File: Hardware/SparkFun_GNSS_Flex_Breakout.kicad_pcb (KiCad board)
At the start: 4 copper layers, 63.5 x 50.8 mm, 194 parts, among them J1 microSD_Friction, J10 USB_C_Receptacle, J11 Conn_02x10, J12 Conn_02x10, J13 JST_Locking_6, J14 Qwiic_Vertical, J2 SMA_Edge, J3 Conn_01x15, J4 Conn_01x18, J5 JST_Locking_6, J6 SMA_Edge, J7 USB_C_Receptacle, J8 U.FL, J9 U.FL, U1 RT9080-3.3, U2 CH342F, U3 74HC4066BQ, U4 AP7361C-3.3V, U5 74HC4066BQ

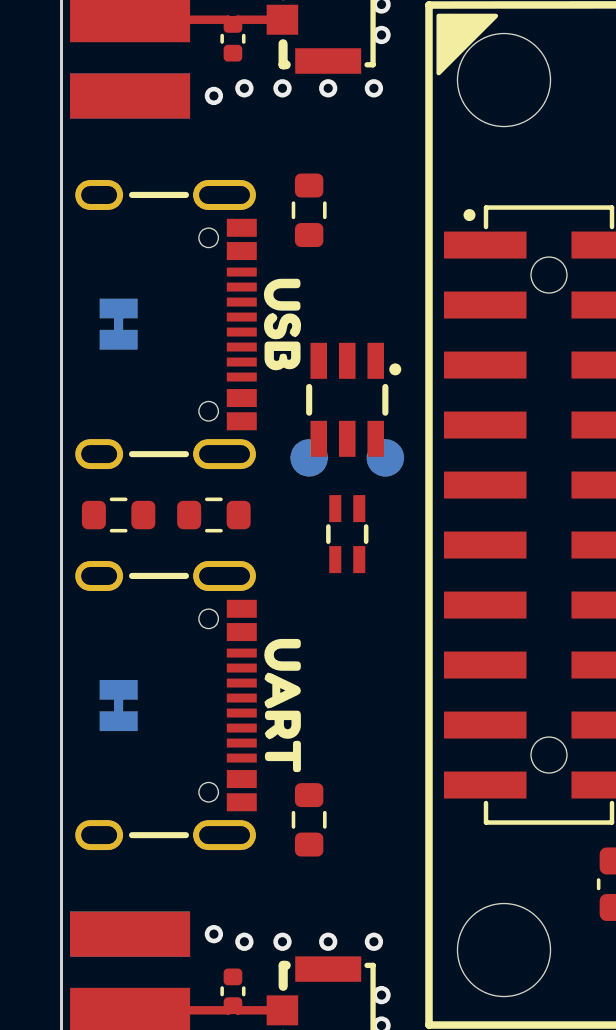
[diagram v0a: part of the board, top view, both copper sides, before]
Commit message: Update QFN-14 3D model. Nudge USB connectors
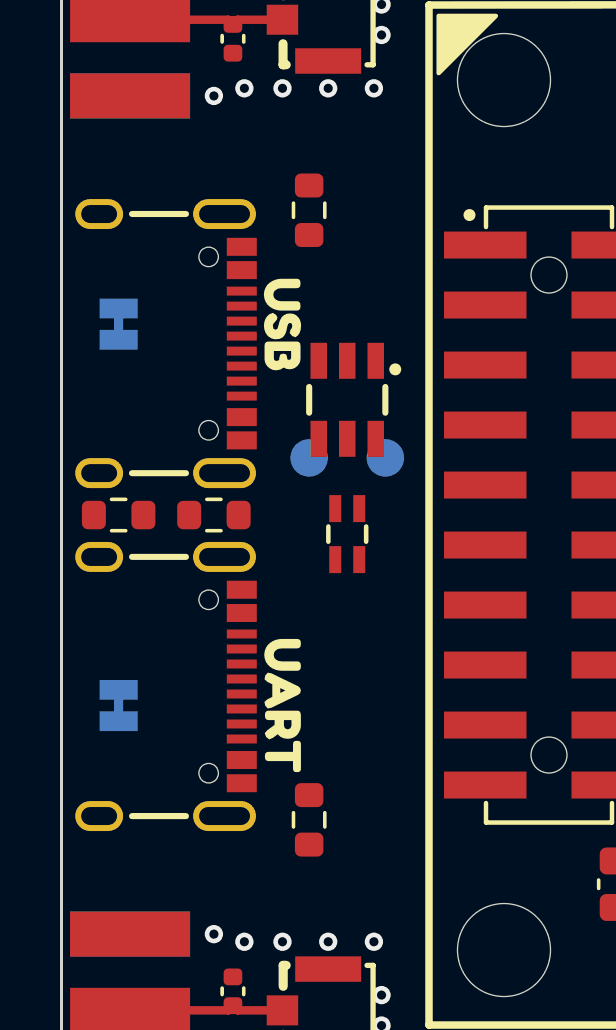
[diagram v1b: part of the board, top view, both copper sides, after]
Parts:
- U3, U5: footprint SparkFun-Semiconductor-Standard:QFN-14_2.5x3mm_P0.5mm -> SparkFun-Semiconductor-Standard:QFN-14_2.5x3mm_P0.5mm_EP1x1.5mm
- moved J10 0.64 mm to (121.9, 93.3)
- moved J7 0.63 mm to (121.9, 104.8)
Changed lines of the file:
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@@
 	(footprint "SparkFun-Connector:USB-C_16"
 		(layer "F.Cu")
-		(at 121.92 92.71 -90)
+		(at 121.92 93.345 -90)
 		(tags "SparkFun")
 		(property "Reference" "J10"
@@
 		)
 		(group ""
-			(members "01ac54b0-38f4-4c66-81d1-e7934c230999" "08e2a2ce-b6c2-4b25-844f-6a4200656d02"
-				"1c49813b-1b20-4e9d-a676-3403a07c5a45" "265d3cdc-5969-47bd-b038-2b6973991091"
-				"8fecda9f-77af-4fc9-bd96-c37ed090db2d" "99adac38-57c6-4b0e-8d9a-73d66b4bb533"
-				"c6655cf9-9159-4c86-91e5-c9e45c30cfb6" "ccf511db-911c-45f6-b676-80cb07481e24"
-				"e62d1002-5302-41e0-ac4a-fce2f966eedc"
+			(members "00169360-e682-4b0c-95a0-17b8250a8605" "176aae39-f481-4c5b-b707-df0a8b82c52c"
+				"38e22b0d-1b0c-4233-bba0-acdcf420ae40" "523512d1-91e7-4edc-a57a-96b930563fc1"
+				"9c7d1eb1-71f1-40b7-8b4f-bf33b49c6e24" "a00d45d5-05e2-44f4-a198-fba7cafcc9a0"
+				"a10154f3-8fa2-4b1c-b6cf-a65719d6ba5e" "a97ac426-b1ec-4fb4-85dc-ff7348ccb279"
+				"f986b6c3-db91-4d3b-af97-8777f0154a02"
 			)
 		)
@@
 		)
 	)
-	(footprint "SparkFun-Semiconductor-Standard:QFN-14_2.5x3mm_P0.5mm"
+	(footprint "SparkFun-Semiconductor-Standard:QFN-14_2.5x3mm_P0.5mm_EP1x1.5mm"
 		(layer "F.Cu")
 		(at 155.305 111.76 -90)
@@
 		)
 		(embedded_fonts no)
-		(model "${SPARKFUN_KICAD_LIBRARY}/Footprints/SparkFun-3D-models/Semiconductor-Standard/QFN-14_2.5x3mm_P0.5mm.step"
+		(model "${SPARKFUN_KICAD_LIBRARY}/Footprints/SparkFun-3D-models/Semiconductor-Standard/QFN-14-1EP_2.5x3.0mm_P0.5mm_EP1.0x1.5mm.step"
 			(offset
 				(xyz 0 0 0)
@@
 			)
 			(rotate
-				(xyz 0 0 0)
+				(xyz -0 -0 -0)
 			)
 		)
@@
 	(footprint "SparkFun-Connector:USB-C_16"
 		(layer "F.Cu")
-		(at 121.92 105.41 -90)
+		(at 121.92 104.775 -90)
 		(tags "SparkFun")
 		(property "Reference" "J7"
@@
 		)
 	)
-	(footprint "SparkFun-Semiconductor-Standard:QFN-14_2.5x3mm_P0.5mm"
+	(footprint "SparkFun-Semiconductor-Standard:QFN-14_2.5x3mm_P0.5mm_EP1x1.5mm"
 		(layer "F.Cu")
 		(at 155.305 100.33 90)
@@
 		)
 		(embedded_fonts no)
-		(model "${SPARKFUN_KICAD_LIBRARY}/Footprints/SparkFun-3D-models/Semiconductor-Standard/QFN-14_2.5x3mm_P0.5mm.step"
+		(model "${SPARKFUN_KICAD_LIBRARY}/Footprints/SparkFun-3D-models/Semiconductor-Standard/QFN-14-1EP_2.5x3.0mm_P0.5mm_EP1.0x1.5mm.step"
 			(offset
 				(xyz 0 0 0)
@@
 			)
 			(rotate
-				(xyz 0 0 0)
+				(xyz -0 -0 -0)
 			)
 		)
@@
 		)
 		(group ""
-			(members "fd960ded-921d-4560-867e-1d624b3082f9")
+			(members "d3058bb2-4b6f-4779-9f0f-f860c11fa2f1")
 		)
 		(embedded_fonts no)
@@
 		)
 		(group ""
-			(members "32ccb73e-8524-49f2-af55-216f90671fd0" "3555361d-09ba-4ea9-a5da-3c5c1199f43c"
-				"5ef2b397-5469-48db-813d-8ca27521d492" "77442049-06ae-4c55-9657-8e4b3c6985f6"
-				"8ab8b8d1-6c3b-491b-9e4e-f22808b68818" "a85bef5d-bfaf-4240-821b-c7702474839e"
-				"c596ca7a-f5e3-415b-855c-0d183b8f1f40" "d0047d29-713f-418f-88cd-fb3f18ed0a38"
-				"f7ec9cab-1ffc-4cf3-8f22-de3bf80f9cbe"
+			(members "12872baf-2d3f-4da6-80b1-310788a44344" "1f7584c4-ab71-4a39-a2f6-afe45f6bb8bf"
+				"5a1d332c-e5c1-43bc-b284-68fbe71df93f" "74049afa-7d02-46fe-b9b9-bf9a416d473c"
+				"87d4d606-e210-46e3-884f-06d16297189e" "88383eb8-c7b6-4f02-8c21-25fb15adaff6"
+				"ceb5f86d-2c23-48d9-8b4b-da604298e7e1" "cfb747da-9703-4d82-afc3-b1726d698b7c"
+				"d7947425-9486-4ed7-9edd-0c3123ef71a4"
 			)
 		)
@@
 		(layer "Dwgs.User")
 		(pts
-			(xy 115.57 92.71) (xy 115.57 82.55)
+			(xy 115.57 93.345) (xy 115.57 82.55)
 		)
 		(height -8.89)
@@
 			(units 0)
 			(units_format 1)
-			(precision 2)
+			(precision 3)
 		)
 		(style
@@
 			(keep_text_aligned yes)
 		)
-		(gr_text "0.40 in"
-			(at 105.53 87.63 90)
+		(gr_text "0.425 in"
+			(at 105.53 87.9475 90)
 			(layer "Dwgs.User")
 			(effects
@@
 		(layer "Dwgs.User")
 		(pts
-			(xy 115.57 105.41) (xy 115.57 92.71)
+			(xy 115.57 104.775) (xy 115.57 93.345)
 		)
 		(height -8.89)
@@
 			(keep_text_aligned yes)
 		)
-		(gr_text "0.50 in"
+		(gr_text "0.45 in"
 			(at 105.53 99.06 90)
 			(layer "Dwgs.User")
@@
 		(layer "Dwgs.User")
 		(pts
-			(xy 115.57 115.57) (xy 115.57 105.41)
+			(xy 115.57 115.57) (xy 115.57 104.775)
 		)
 		(height -8.89)
@@
 			(units 0)
 			(units_format 1)
-			(precision 2)
+			(precision 3)
 		)
 		(style
@@
 			(keep_text_aligned yes)
 		)
-		(gr_text "0.40 in"
-			(at 105.53 110.49 90)
+		(gr_text "0.425 in"
+			(at 105.53 110.1725 90)
 			(layer "Dwgs.User")
 			(effects

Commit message: Routing WIP
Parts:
- removed TR1: RFCMF1220100M4T, SparkFun-Coil:RFCMF1220100M4T
- removed the kibuzzard-67E6B983 at (163.2, 79.4)
- removed kibuzzard-67E6BA22: G***, kibuzzard-67E6BA22
- removed kibuzzard-67E6BAF6: G***, kibuzzard-67E6BAF6
- added G***: LOGO, SparkFun-Aesthetic:qwiic_4mm, F.Cu at (135.3, 78.5)
- added VBATT.1: ~, SparkFun-Jumper:Jumper_2_NC_Trace, B.Cu at (141.6, 92.1)
- added kibuzzard-67EE9E3C: G***, kibuzzard-67EE9E3C, B.Cu at (141.6, 87.5)
- added kibuzzard-67EE9EE3: G***, kibuzzard-67EE9EE3, F.Cu at (127.0, 84.8)
- added kibuzzard-67EE9EE3: G***, kibuzzard-67EE9EE3, B.Cu at (120.8, 82.7)
- added kibuzzard-67EE9EFF: G***, kibuzzard-67EE9EFF, F.Cu at (127.0, 113.3)
- added kibuzzard-67EE9EFF: G***, kibuzzard-67EE9EFF, B.Cu at (120.8, 115.8)
- added kibuzzard-67EEB400: G***, kibuzzard-67EEB400, F.Cu at (143.5, 77.0)
- added kibuzzard-67EEB40C: G***, kibuzzard-67EEB40C, B.Cu at (143.5, 77.0)
- moved kibuzzard-67D171AB 3.58 mm to (144.8, 108.0)
- moved TP12 3.58 mm to (146.1, 108.0)
- moved kibuzzard-67E6B983 3.53 mm to (160.0, 82.4), turned to 180 degrees
- moved kibuzzard-67D171E5 2.78 mm to (144.8, 104.1)
- moved TP9 2.78 mm to (146.1, 104.1)
- moved D17 0.43 mm to (144.1, 106.0), turned to 180 degrees
- moved C14 0.40 mm to (158.8, 112.1)
- moved U5 0.38 mm to (155.3, 112.1)
- moved U2 0.18 mm to (155.3, 106.2)
- moved D14 0.13 mm to (175.9, 113.5), turned to 90 degrees
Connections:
- C21 pad 1: VBATT -> Net-(U1-VOUT)
- C22 pad 1: VBATT -> Net-(U1-VOUT)
- D17 pad 1: Net-(D17-I/O1) -> USB2_D-
- D17 pad 3: Net-(D17-I/O2) -> USB2_D+
- D17 pad 4: Net-(D17-I/O2) -> USB2_D+
- D17 pad 6: Net-(D17-I/O1) -> USB2_D-
- J7 pad A6: Net-(D17-I/O2) -> USB2_D+
- J7 pad A7: Net-(D17-I/O1) -> USB2_D-
- J7 pad B6: Net-(D17-I/O2) -> USB2_D+
- J7 pad B7: Net-(D17-I/O1) -> USB2_D-
- TP12 pad 1: Net-(D17-I/O1) -> USB2_D-
- TP9 pad 1: Net-(D17-I/O2) -> USB2_D+
- U1 pad 5: VBATT -> Net-(U1-VOUT)
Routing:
- net RX1: track 0.00 -> 84.0 mm, vias 0 -> 7
- net 5V: track 0.00 -> 82.2 mm, vias 0 -> 2
- net VUSB2: track 0.00 -> 78.8 mm, vias 0 -> 7
- net CTS1: track 0.00 -> 78.0 mm, vias 0 -> 8
- net TX1: track 0.00 -> 76.5 mm, vias 0 -> 6
- net RTS1: track 0.00 -> 74.8 mm, vias 0 -> 7
- net RX2: track 0.00 -> 71.3 mm, vias 0 -> 4
- net RTS2: track 0.00 -> 66.0 mm, vias 0 -> 4
- net TX2: track 0.00 -> 62.5 mm, vias 0 -> 4
- net CTS2: track 0.00 -> 62.1 mm, vias 0 -> 6
- net VUSB1: track 0.00 -> 58.7 mm, vias 0 -> 6
- net USB2_D-: track 0.00 -> 38.7 mm, vias 0 -> 3
- net ID: track 0.00 -> 37.1 mm, vias 0 -> 1
- net USB2_D+: track 0.00 -> 36.9 mm, vias 0 -> 3
- net 3.3V: track 0.00 -> 33.0 mm, vias 0 -> 10
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- added copper zone on In2.Cu, net 3.3V

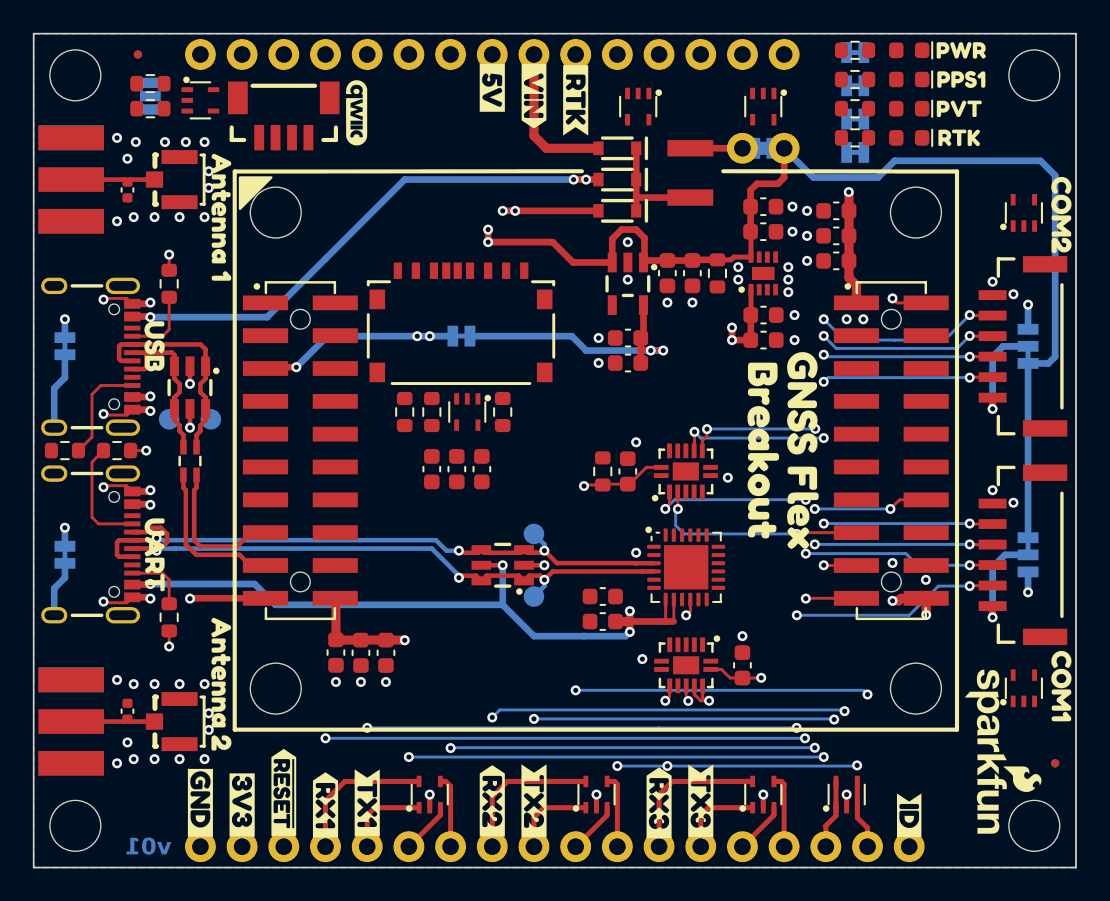
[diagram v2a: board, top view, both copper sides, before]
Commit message: Routed and panelized
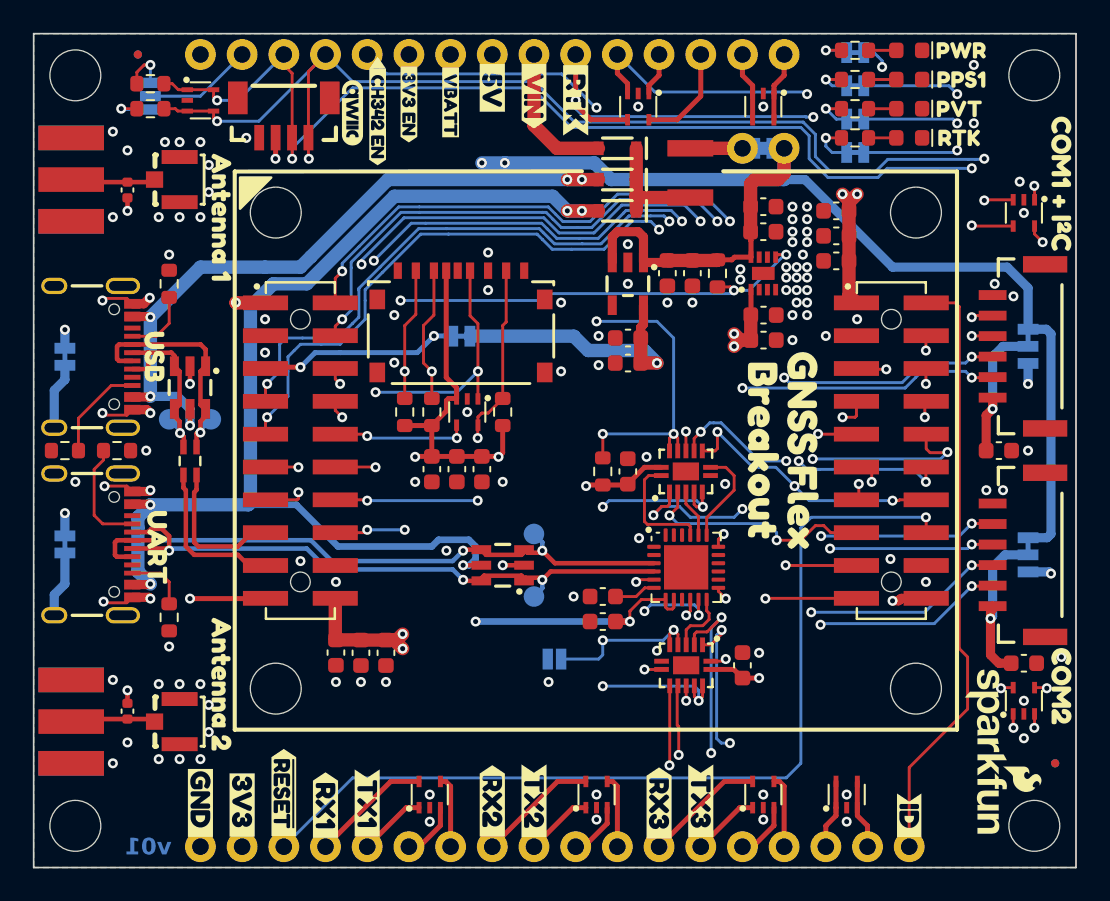
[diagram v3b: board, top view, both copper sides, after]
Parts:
- removed kibuzzard-67D04D99: G***, kibuzzard-67D04D99
- removed kibuzzard-67E6AD83: G***, kibuzzard-67E6AD83
- removed kibuzzard-67E6AD9C: G***, kibuzzard-67E6AD9C
- removed kibuzzard-67E6AFB1 (x2): G***, kibuzzard-67E6AFB1
- removed kibuzzard-67E6AFE8 (x2): G***, kibuzzard-67E6AFE8
- added C23: 10uF, SparkFun-Capacitor:C_0603_1608Metric, F.Cu at (175.9, 112.0)
- added C24: 10uF, SparkFun-Capacitor:C_0603_1608Metric, F.Cu at (174.4, 99.1)
- added CH342_EN.1: ~, SparkFun-Jumper:Jumper_2_NO, B.Cu at (147.3, 111.8)
- added kibuzzard-67E6AD12: G***, kibuzzard-67E6AD12, B.Cu at (176.1, 96.3)
- added kibuzzard-67E6AD3C: G***, kibuzzard-67E6AD3C, B.Cu at (176.1, 89.5)
- added kibuzzard-67EFA2E8: G***, kibuzzard-67EFA2E8, B.Cu at (178.2, 105.4)
- added kibuzzard-67EFA2F1: G***, kibuzzard-67EFA2F1, F.Cu at (178.2, 113.4)
- added kibuzzard-67EFDDCD: G***, kibuzzard-67EFDDCD, B.Cu at (141.0, 78.6)
- added kibuzzard-67EFDDEA: G***, kibuzzard-67EFDDEA, F.Cu at (141.0, 77.9)
- added kibuzzard-67EFDE19: G***, kibuzzard-67EFDE19, F.Cu at (138.4, 78.0)
- added kibuzzard-67EFDE56: G***, kibuzzard-67EFDE56, F.Cu at (136.5, 78.7)
- added kibuzzard-67EFEB6F: G***, kibuzzard-67EFEB6F, F.Cu at (178.2, 82.8)
- added kibuzzard-67EFEB92: G***, kibuzzard-67EFEB92, B.Cu at (178.2, 92.7)
- added kibuzzard-67EFED19: G***, kibuzzard-67EFED19, B.Cu at (142.4, 111.8)
- moved VOUT1 12.7 mm to (176.1, 92.7)
- moved VOUT2 12.7 mm to (176.1, 105.4), turned to -90 degrees
- moved D14 0.76 mm to (175.9, 114.3)
- moved SHLD1 0.65 mm to (117.5, 93.3)
- moved kibuzzard-67E6B1CF 0.65 mm to (121.0, 93.3)
- moved kibuzzard-67E6B1E0 0.65 mm to (121.0, 104.8)
- moved kibuzzard-67D05112 0.64 mm to (119.1, 93.3)
- moved kibuzzard-67E6B1CF 0.64 mm to (122.9, 93.3)
- moved SHLD2 0.63 mm to (117.5, 104.8)
- moved kibuzzard-67D05112 0.63 mm to (119.1, 104.8)
- moved kibuzzard-67E6B1E0 0.48 mm to (123.1, 105.0)
- moved G*** 0.25 mm to (135.0, 78.5)
- turned D16 to -90 degrees
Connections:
- D14 pad 1: RX1 -> RX2
- D14 pad 3: CTS1 -> CTS2
- D14 pad 4: RTS1 -> RTS2
- D14 pad 5: TX1 -> TX2
- D16 pad 1: RX2 -> TX1
- D16 pad 3: CTS2 -> SCL
- D16 pad 4: RTS2 -> SDA
- D16 pad 5: TX2 -> RX1
- J13 pad 2: TX2 -> RX1
- J13 pad 3: RX2 -> TX1
- J13 pad 4: CTS2 -> SCL
- J13 pad 5: RTS2 -> SDA
- J5 pad 2: TX1 -> TX2
- J5 pad 3: RX1 -> RX2
- J5 pad 4: CTS1 -> CTS2
- J5 pad 5: RTS1 -> RTS2
- VOUT1 pad 2: Net-(J5-Pin_1) -> Net-(J13-Pin_1)
- VOUT2 pad 2: Net-(J13-Pin_1) -> Net-(J5-Pin_1)
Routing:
- net SCL: track 0.00 -> 101.3 mm, vias 0 -> 6
- net SDA: track 0.00 -> 97.8 mm, vias 0 -> 6
- net CH342_EN: track 2.49 -> 90.2 mm, vias 1 -> 10
- net RTK_LED: track 0.00 -> 86.0 mm, vias 0 -> 5
- net PVT_LED: track 0.00 -> 75.3 mm, vias 0 -> 4
- net PPS1: track 0.00 -> 63.2 mm, vias 0 -> 3
- net ~{RESET}: track 0.00 -> 56.8 mm, vias 0 -> 1
- net EVENT_A: track 0.00 -> 48.8 mm, vias 0 -> 3
- net EVENT_B: track 0.00 -> 45.9 mm, vias 0 -> 3
- net PPS2: track 0.00 -> 45.4 mm, vias 0 -> 2
- net RTS3: track 3.17 -> 45.4 mm, vias 0 -> 1
- net 3V3_EN: track 0.00 -> 41.7 mm, vias 0 -> 3
- net CTS3: track 4.50 -> 42.7 mm, vias 0 -> 1
- net TX3: track 5.26 -> 43.5 mm, vias 0 -> 1
- net RX3: track 9.21 -> 45.0 mm, vias 0 -> 1
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
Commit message: Updates after proto review
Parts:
- removed VBATT.1: ~, SparkFun-Jumper:Jumper_2_NC_Trace
- removed kibuzzard-67D04A61: G***, kibuzzard-67D04A61
- removed kibuzzard-67D04A91: G***, kibuzzard-67D04A91
- removed kibuzzard-67D04AA3: G***, kibuzzard-67D04AA3
- removed kibuzzard-67E686F1: G***, kibuzzard-67E686F1
- removed kibuzzard-67EE9E3C: G***, kibuzzard-67EE9E3C
- removed kibuzzard-67EFDDEA: G***, kibuzzard-67EFDDEA
- removed kibuzzard-67EFDE19: G***, kibuzzard-67EFDE19
- removed kibuzzard-67EFED19: G***, kibuzzard-67EFED19
- added J15: Legend: GNSS Flex, SparkFun-Aesthetic:GNSS_Flex_Template, F.Cu at (149.8, 99.1)
- added VBACKUP.1: ~, SparkFun-Jumper:Jumper_2_NC_Trace, B.Cu at (141.6, 92.1)
- added kibuzzard-67D044ED: G***, kibuzzard-67D044ED, F.Cu at (171.4, 120.5)
- added kibuzzard-67D045AD: G***, kibuzzard-67D045AD, B.Cu at (171.4, 120.5)
- added kibuzzard-67F7ADB8: G***, kibuzzard-67F7ADB8, B.Cu at (141.6, 87.2)
- added kibuzzard-67F7B6D2: G***, kibuzzard-67F7B6D2, F.Cu at (141.0, 77.9)
- added kibuzzard-67F7B6D7: G***, kibuzzard-67F7B6D7, F.Cu at (138.4, 78.0)
- added kibuzzard-67F7B700: G***, kibuzzard-67F7B700, F.Cu at (156.2, 77.5)
- added kibuzzard-67F7C8FB: G***, kibuzzard-67F7C8FB, B.Cu at (142.4, 111.8)
- added kibuzzard-67F7C94B: G***, kibuzzard-67F7C94B, B.Cu at (169.2, 74.8)
- added kibuzzard-67F7C969: G***, kibuzzard-67F7C969, B.Cu at (169.2, 76.8)
- added kibuzzard-67F7C97D: G***, kibuzzard-67F7C97D, B.Cu at (169.0, 78.9)
- added kibuzzard-67F7C991: G***, kibuzzard-67F7C991, B.Cu at (168.9, 80.9)
- J4: footprint SparkFun-Connector:1x18 -> SparkFun-Connector:1x19
- moved R19 13.7 mm to (125.3, 87.9), turned to -90 degrees
- moved C24 13.0 mm to (175.9, 86.1)
- moved R18 12.1 mm to (125.3, 110.2), turned to 90 degrees
- moved R17 1.02 mm to (123.8, 110.2)
- moved R20 1.02 mm to (123.8, 87.9)
- moved D16 0.77 mm to (176.0, 83.8)
- turned kibuzzard-67D1674C to 0 degrees
- turned kibuzzard-67D16775 to 0 degrees
- turned kibuzzard-67E68821 to 0 degrees
- turned kibuzzard-67E68BE1 to 0 degrees
- turned kibuzzard-67E6B983 to 0 degrees
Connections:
- net VBATT renamed VBACKUP
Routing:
- net Net-(J7-CC1): track 6.72 -> 18.2 mm, vias 0 -> 2
- net Net-(J13-Pin_1): track 8.99 -> 17.4 mm
- net Net-(J10-CC2): track 6.08 -> 9.66 mm, vias 0 -> 2
- net 5V: track 84.3 -> 85.9 mm
- net TX1: track 94.6 -> 96.2 mm
- net RX1: track 99.6 -> 101.1 mm
- net RX2: track 89.7 -> 90.9 mm
- net Net-(J7-CC2): track 3.80 -> 4.82 mm
- net Net-(J10-CC1): track 4.16 -> 5.17 mm
- net PPS2: track 45.4 -> 44.6 mm
- net PPS1: track 63.2 -> 62.4 mm
- net PVT_LED: track 75.3 -> 76.1 mm
- net GND: vias 122 -> 127
